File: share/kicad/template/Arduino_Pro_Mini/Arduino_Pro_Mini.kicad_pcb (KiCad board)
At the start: 2 copper layers, 17.8 x 33 mm, 5 parts, among them P1 Digital, P2 COM, P3 ADC, P4 Analog, P5 ADC

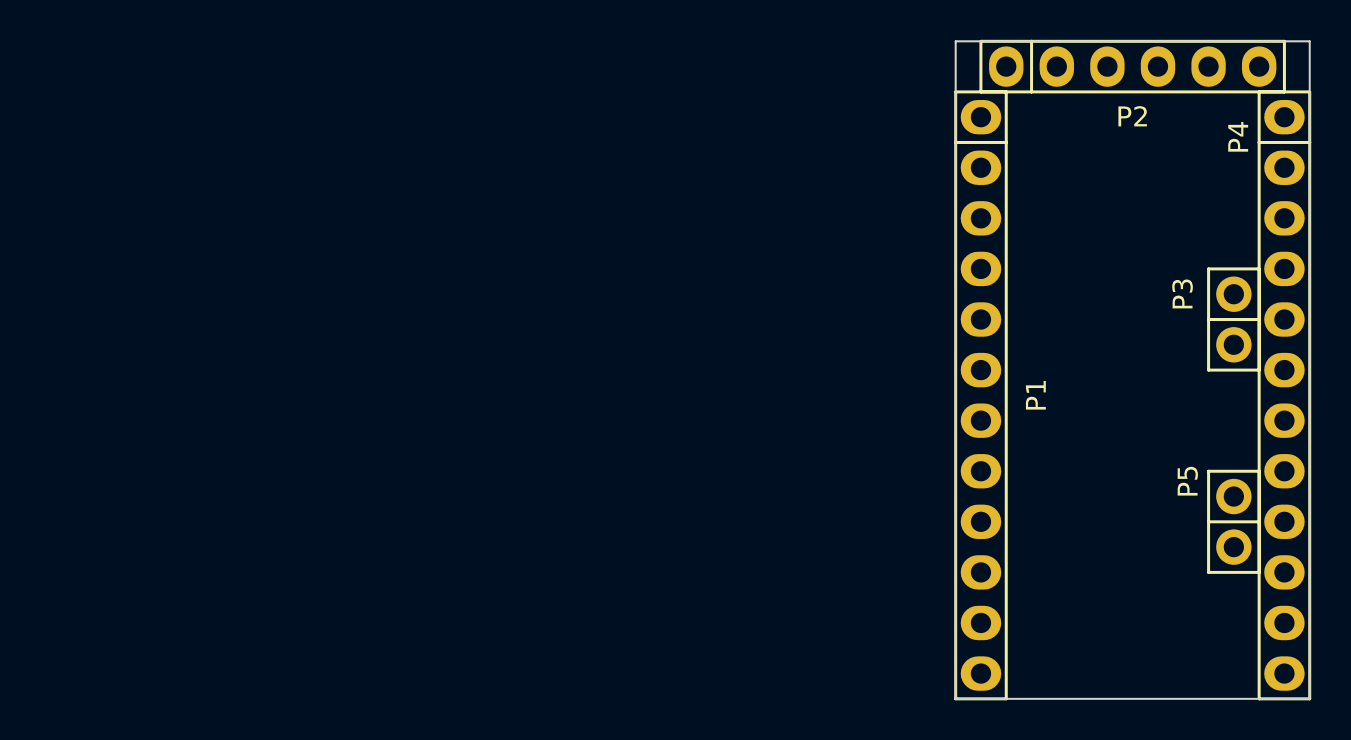
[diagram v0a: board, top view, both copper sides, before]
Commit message: Remove KiCad V4.0.7
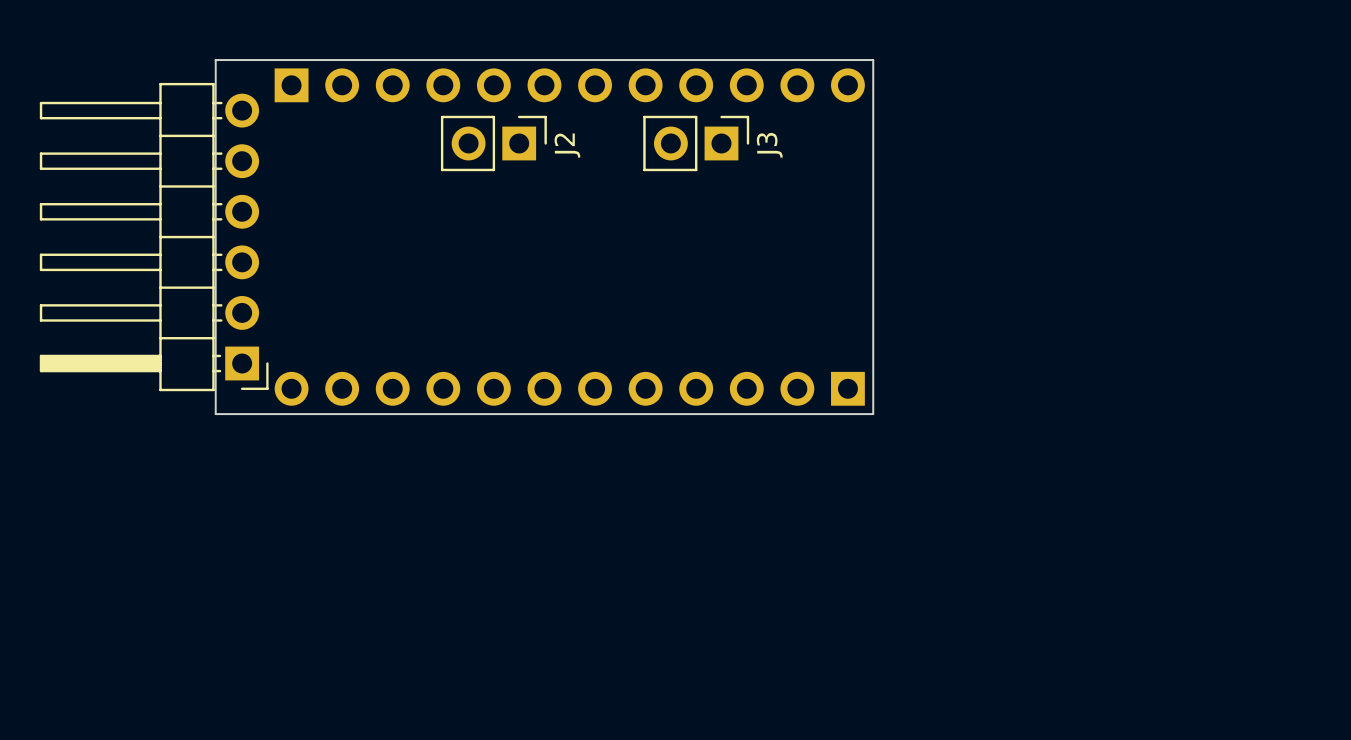
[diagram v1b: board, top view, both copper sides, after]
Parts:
- removed P1: Digital, Socket_Arduino_Pro_Mini:Socket_Strip_Arduino_1x12
- removed P2: COM, Socket_Arduino_Pro_Mini:Socket_Strip_Arduino_1x06
- removed P3, P5: ADC, Socket_Arduino_Pro_Mini:Socket_Strip_Arduino_1x02
- removed P4: Analog, Socket_Arduino_Pro_Mini:Socket_Strip_Arduino_1x12
- added J1: FTDI, Connector_PinHeader_2.54mm:PinHeader_1x06_P2.54mm_Horizontal, F.Cu at (101.3, 97.5)
- added J2: I2C, Connector_PinHeader_2.54mm:PinHeader_1x02_P2.54mm_Vertical, F.Cu at (115.2, 86.4)
- added J3: Analog, Connector_PinHeader_2.54mm:PinHeader_1x02_P2.54mm_Vertical, F.Cu at (125.4, 86.4)
- added J6: Digital, Connector_PinHeader_2.54mm:PinHeader_1x12_P2.54mm_Vertical, B.Cu at (103.8, 83.5)
- added J7: Analog, Connector_PinHeader_2.54mm:PinHeader_1x12_P2.54mm_Vertical, B.Cu at (131.8, 98.7)
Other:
- board size 17.8 x 33 mm -> 33 x 17.8 mm
- net class Default removed
- board text removed: "1"
